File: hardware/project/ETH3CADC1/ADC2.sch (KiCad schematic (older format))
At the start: 45 parts, among them U401 DG211B, U402 OPA2192, U403 DG419xY, U404 LT5400-100k-100k, U405 LT5400-5k-1k, U406 OPA177, U407 OPA140, U408 OPA192, U409 LT5400-10k-10k, U410 LM311

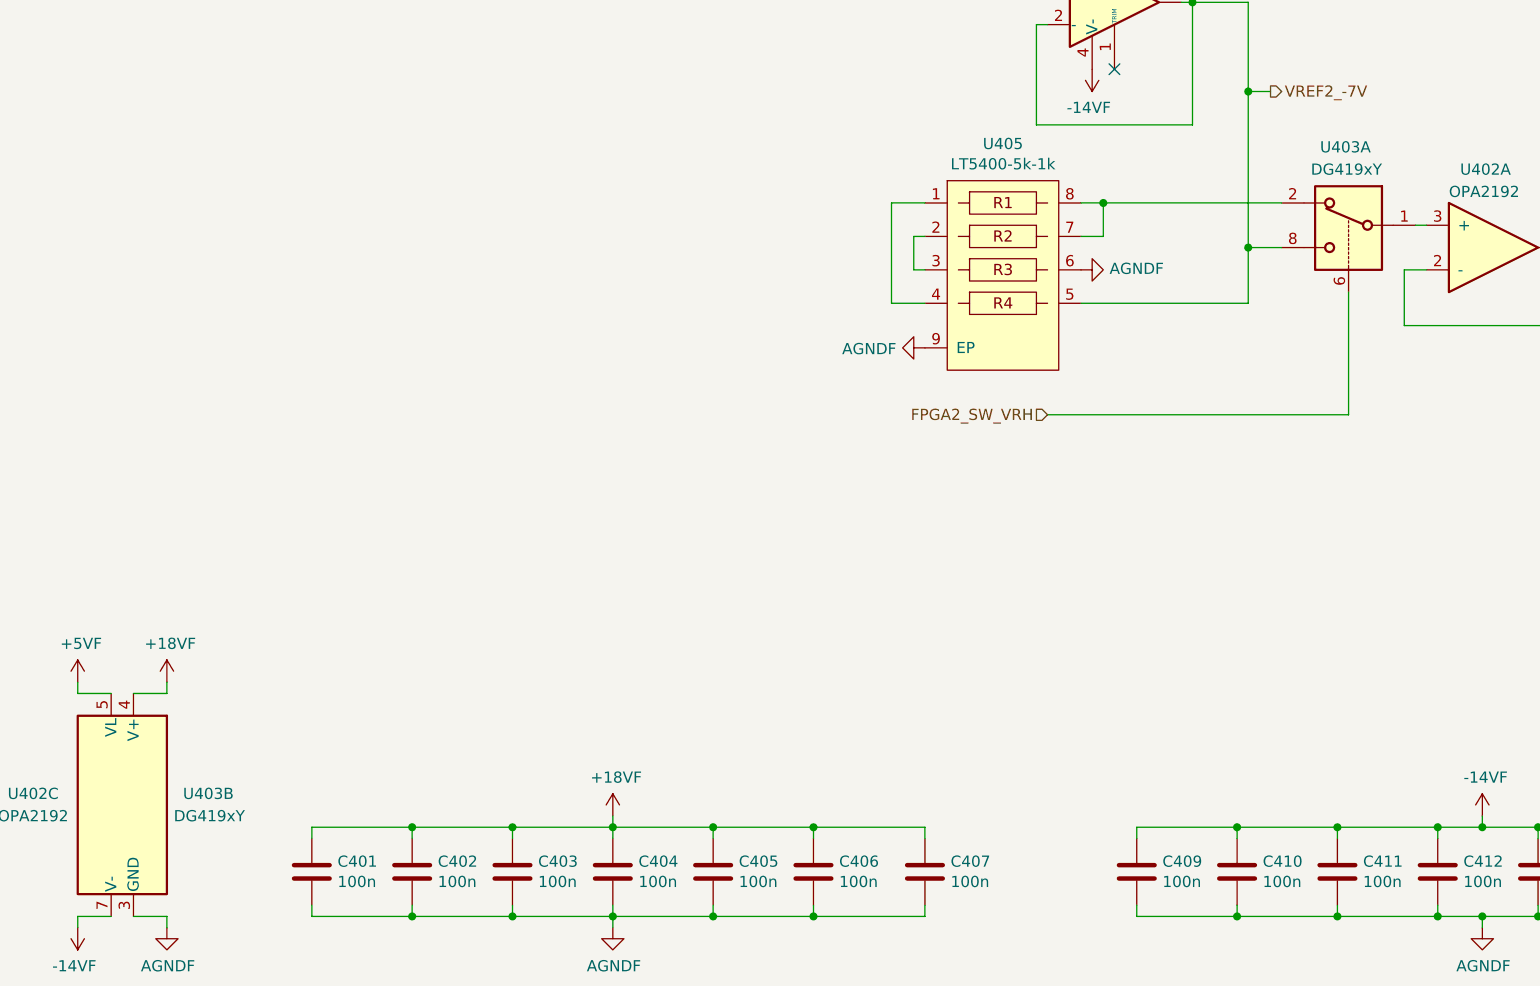
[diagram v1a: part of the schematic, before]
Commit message: Fixed mistake with DG419. Never use DG419Lxx variant.
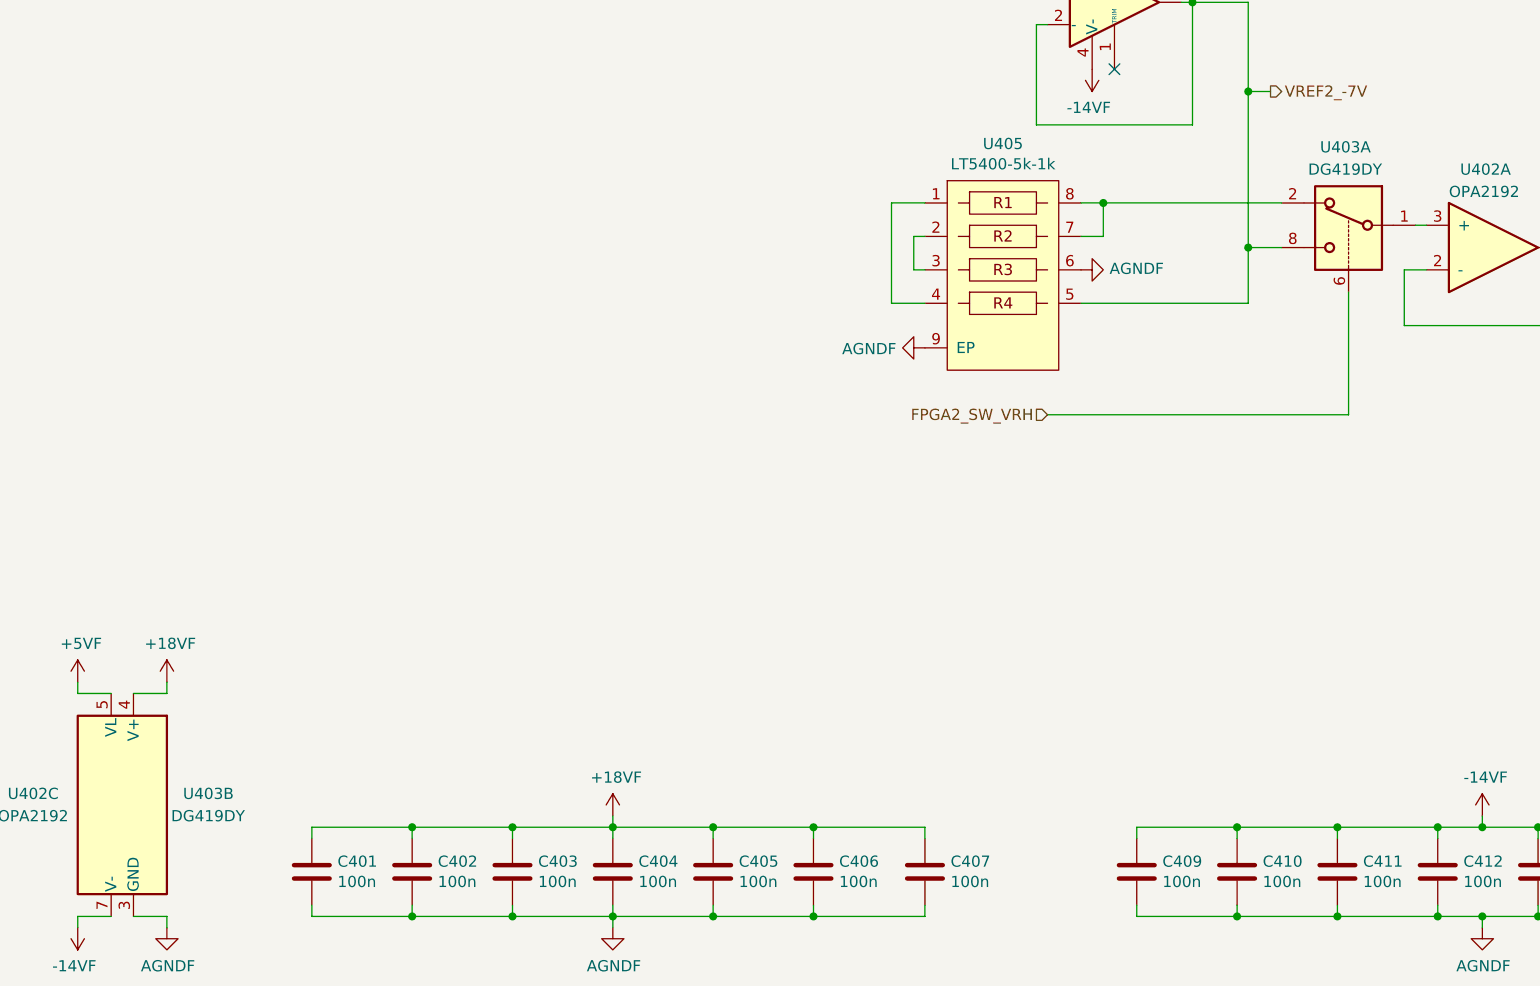
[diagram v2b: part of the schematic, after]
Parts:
- U403: value DG419xY -> DG419DY
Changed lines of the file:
@@
 AR Path="/605B15BF/6032E920" Ref="U?"  Part="1"
 F 0 "U403" H 8050 7650 50  0000 L CNN
-F 1 "DG419xY" H 8000 7550 50  0000 L CNN
+F 1 "DG419DY" H 8000 7550 50  0000 L CNN
 F 2 "Package_SO:SOIC-8_3.9x4.9mm_P1.27mm" H 8150 7100 50  0001 C CNN
 F 3 "https://datasheets.maximintegrated.com/en/ds/DG417-DG419.pdf" H 8150 7400 50  0001 C CNN
@@
 AR Path="/605B15BF/6032E9AE" Ref="U?"  Part="2"
 F 0 "U403" H 2250 10150 50  0000 L CNN
-F 1 "DG419xY" H 2200 10050 50  0000 L CNN
+F 1 "DG419DY" H 2200 10050 50  0000 L CNN
 F 2 "Package_SO:SOIC-8_3.9x4.9mm_P1.27mm" H 2700 9800 50  0001 C CNN
 F 3 "https://datasheets.maximintegrated.com/en/ds/DG417-DG419.pdf" H 2700 10100 50  0001 C CNN

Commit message: Development
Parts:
- removed C401, C402, C403, C404, C405, C406, C407, C409, C410, C411, C412, C414, C416, C417, C418, C419, C420, C421: 100n, Capacitor_SMD:C_0402_1005Metric_Pad0.74x0.62mm_HandSolder, symbol Device:C
- removed C408: 2n2/SMD, Capacitor_SMD:C_0603_1608Metric_Pad1.08x0.95mm_HandSolder, symbol Device:C
- removed C413: 33p, Capacitor_SMD:C_0402_1005Metric_Pad0.74x0.62mm_HandSolder, symbol Device:C
- removed C415: DNP, Capacitor_SMD:C_0402_1005Metric_Pad0.74x0.62mm_HandSolder, symbol Device:C
- removed D401, D402: BAV21W, Diode_SMD:D_SOD-123, symbol Device:D
- removed R401, R402, R404, R405, R409: 10, Resistor_SMD:R_0402_1005Metric_Pad0.72x0.64mm_HandSolder, symbol Device:R
- removed R403: 12k/.05%, Resistor_SMD:R_0603_1608Metric_Pad0.98x0.95mm_HandSolder, symbol Device:R
- removed R406: 62k, Resistor_SMD:R_0402_1005Metric_Pad0.72x0.64mm_HandSolder, symbol Device:R
- removed R407: 620/.05%, Resistor_SMD:R_0603_1608Metric_Pad0.98x0.95mm_HandSolder, symbol Device:R
- removed R408, R412: 3k9/.05%, Resistor_SMD:R_0603_1608Metric_Pad0.98x0.95mm_HandSolder, symbol Device:R
- removed R410: 62/.1%, Resistor_SMD:R_0603_1608Metric_Pad0.98x0.95mm_HandSolder, symbol Device:R
- removed R411: 39k/.05%, Resistor_SMD:R_0603_1608Metric_Pad0.98x0.95mm_HandSolder, symbol Device:R
- removed U401: DG211B, Package_SO:TSSOP-16_4.4x5mm_P0.65mm, symbol ETH3CDAQ1:DG211
- removed U402: OPA2192, Package_SO:SOIC-8_3.9x4.9mm_P1.27mm, symbol ETH3CDAQ1:OPA2192
- removed U403: DG419DY, Package_SO:SOIC-8_3.9x4.9mm_P1.27mm, symbol Analog_Switch:DG419xY
- removed U404: LT5400-100k-100k, Package_SO:MSOP-8-1EP_3x3mm_P0.65mm_EP1.73x1.85mm_ThermalVias, symbol ETH3CDAQ1:LT5400-100k-100k
- removed U405: LT5400-5k-1k, Package_SO:MSOP-8-1EP_3x3mm_P0.65mm_EP1.73x1.85mm_ThermalVias, symbol ETH3CDAQ1:LT5400-5k-1k
- removed U406: OPA177, Package_SO:SOIC-8_3.9x4.9mm_P1.27mm, symbol ETH3CDAQ1:OPA177
- removed U407: OPA140, Package_SO:SOIC-8_3.9x4.9mm_P1.27mm, symbol ETH3CDAQ1:OPA140
- removed U408: OPA192, Package_SO:SOIC-8_3.9x4.9mm_P1.27mm, symbol ETH3CDAQ1:OPA192
- removed U409: LT5400-10k-10k, Package_SO:MSOP-8-1EP_3x3mm_P0.65mm_EP1.73x1.85mm_ThermalVias, symbol ETH3CDAQ1:LT5400-10k-10k
- removed U410: LM311, Package_SO:SOIC-8_3.9x4.9mm_P1.27mm, symbol Comparator:LM311
- added C1401, C1402, C1403, C1404, C1405, C1406, C1407, C1408, C1409, C1411, C1412, C1413, C1414, C1415, C1417, C1418, C1419, C1420, C1421: 100n, Capacitor_SMD:C_0402_1005Metric_Pad0.74x0.62mm_HandSolder, symbol Device:C
- added C1410: 2n2/SMD, Capacitor_SMD:C_0603_1608Metric_Pad1.08x0.95mm_HandSolder, symbol Device:C
- added C1416: 33p, Capacitor_SMD:C_0402_1005Metric_Pad0.74x0.62mm_HandSolder, symbol Device:C
- added D1401, D1402: BAV21W, Diode_SMD:D_SOD-123, symbol Device:D
- added R1401, R1402, R1403, R1404, R1407: 10k, Resistor_SMD:R_0402_1005Metric_Pad0.72x0.64mm_HandSolder, symbol Device:R
- added R1405: 10M, Resistor_SMD:R_0603_1608Metric_Pad0.98x0.95mm_HandSolder, symbol Device:R
- added R1406: 0, Resistor_SMD:R_0402_1005Metric_Pad0.72x0.64mm_HandSolder, symbol Device:R
- added R1408, R1418: 62/.1%, Resistor_SMD:R_0603_1608Metric_Pad0.98x0.95mm_HandSolder, symbol Device:R
- added R1409, R1410, R1412, R1413, R1417: 10, Resistor_SMD:R_0402_1005Metric_Pad0.72x0.64mm_HandSolder, symbol Device:R
- added R1411: 12k/.05%, Resistor_SMD:R_0603_1608Metric_Pad0.98x0.95mm_HandSolder, symbol Device:R
- added R1414: 62k, Resistor_SMD:R_0402_1005Metric_Pad0.72x0.64mm_HandSolder, symbol Device:R
- added R1415: 620/.05%, Resistor_SMD:R_0603_1608Metric_Pad0.98x0.95mm_HandSolder, symbol Device:R
- added R1416, R1420: 3k9/.05%, Resistor_SMD:R_0603_1608Metric_Pad0.98x0.95mm_HandSolder, symbol Device:R
- added R1419: 39k/.05%, Resistor_SMD:R_0603_1608Metric_Pad0.98x0.95mm_HandSolder, symbol Device:R
- added U1401: DG211, Package_SO:TSSOP-16_4.4x5mm_P0.65mm, symbol ETH3CDAQ1:DG211
- added U1402: DG211B, Package_SO:TSSOP-16_4.4x5mm_P0.65mm, symbol ETH3CDAQ1:DG211
- added U1403: OPA2192, Package_SO:SOIC-8_3.9x4.9mm_P1.27mm, symbol ETH3CDAQ1:OPA2192
- added U1404: DG419DY, Package_SO:SOIC-8_3.9x4.9mm_P1.27mm, symbol Analog_Switch:DG419xY
- added U1405, U1409: OPA140, Package_SO:SOIC-8_3.9x4.9mm_P1.27mm, symbol ETH3CDAQ1:OPA140
- added U1406: LT5400-100k-100k, Package_SO:MSOP-8-1EP_3x3mm_P0.65mm_EP1.73x1.85mm_ThermalVias, symbol ETH3CDAQ1:LT5400-100k-100k
- added U1407: LT5400-5k-1k, Package_SO:MSOP-8-1EP_3x3mm_P0.65mm_EP1.73x1.85mm_ThermalVias, symbol ETH3CDAQ1:LT5400-5k-1k
- added U1408: OPA177, Package_SO:SOIC-8_3.9x4.9mm_P1.27mm, symbol ETH3CDAQ1:OPA177
- added U1410: LT5400-10k-10k, Package_SO:MSOP-8-1EP_3x3mm_P0.65mm_EP1.73x1.85mm_ThermalVias, symbol ETH3CDAQ1:LT5400-10k-10k
- added U1411: OPA192, Package_SO:SOIC-8_3.9x4.9mm_P1.27mm, symbol ETH3CDAQ1:OPA192
- added U1412: LM311, Package_SO:SOIC-8_3.9x4.9mm_P1.27mm, symbol Comparator:LM311
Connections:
- net +18VF: now also C1401.1, C1402.1, C1403.1, C1405.1, C1406.1, C1407.1, C1408.1, R1409.1, R1412.1, U1401.13 (V+), U1402.13 (V+), U1403.4 (V-), U1404.4 (V+), U1405.7 (V+), U1408.7 (V+)
- net -14VF: now also C1409.1, C1411.1, C1412.1, C1413.1, C1414.1, C1415.1, C1417.1, C1418.1, R1410.2, R1413.2, R1417.2, U1401.4 (V-), U1402.4 (V-), U1403.8 (V+), U1404.7 (V-), U1405.4 (V-), U1408.4 (V-)
- net ADIN2: now also R1401.2
- net AD_COMP2: now also R1420.2, U1412.7
- net AGNDF: now also C1401.2, C1402.2, C1403.2, C1404.2, C1405.2, C1406.2, C1407.2, C1408.2, C1409.2, C1411.2, C1412.2, C1413.2, C1414.2, C1415.2, C1417.2, C1418.2, R1402.2, R1405.2, R1415.2, U1401.5 (GND), U1402.5 (GND), U1403.6 (-), U1404.3 (GND), U1406.9 (EP), U1407.6, U1407.9 (EP), U1409.3 (+), U1410.9 (EP), U1411.3 (+)
- net DGNDF: now also C1419.2, C1420.2, U1412.1 (GND)
- net FGPA2_AD_ID: now also U1402.16
- net FGPA2_AD_IIN: now also U1402.1
- net FGPA2_AD_IRN: now also U1402.8
- net FGPA2_AD_IRP: now also U1402.9
- net FPGA2_SW_VRH: now also U1404.6
- net VREF+: now also U1403.7, U1406.4, U1410.1, U1410.2
- net VREF-: now also U1403.1, U1403.2 (-), U1406.3, U1410.3, U1410.4
- net VREF_N7V_LPF: now also R1404.2, R1408.2
- new net: R1406.1, R1407.2, U1405.2 (-), U1405.6
- new net: R1405.1, R1406.2, U1401.10, U1401.15, U1401.3, U1401.6, U1405.3 (+)
- new net: U1402.6, U1406.5
- new net: C1410.2, U1402.10, U1402.14, U1402.3, U1402.7, U1409.2 (-)
- new net: U1402.11, U1406.6
- new net: U1403.5 (+), U1410.5, U1410.6, U1410.7, U1410.8
- new net: C1410.1, R1411.2, U1402.15, U1409.6
- new net: U1403.3 (+), U1404.1
- new net: U1407.1, U1407.4
- new net: U1407.2, U1407.3
- new net: U1404.8, U1407.5, U1408.2 (-), U1408.6
- new net: U1404.2, U1407.7, U1407.8
- new net: C1416.2, D1401.2 (A), D1402.1 (K), R1411.1, R1414.2, U1411.2 (-)
- new net: R1413.1, U1411.4 (V-)
- new net: C1416.1, D1401.1 (K), D1402.2 (A), R1414.1, R1416.2, U1411.6
- new net: R1412.2, U1411.7 (V+)
- new net: R1401.1, U1401.2
- new net: R1404.1, U1401.14
- new net: R1403.1, U1401.11
- new net: R1402.1, U1401.7
- new net: C1404.1, R1408.1, U1408.3 (+)
- new net: R1410.1, U1409.4 (V-)
- new net: R1409.2, U1409.7 (V+)
- new net: R1407.1, U1406.8
- new net: R1415.1, U1412.3 (-)
- new net: C1421.2, R1417.1, U1412.4 (V-)
- new net: R1418.2, R1419.1, R1420.1
- new net: R1419.2, U1412.5 (BAL)
- new net: U1406.1, U1406.2
- new net: U1402.2, U1406.7
- new net: R1416.1, U1412.2 (+)
- new net +10VRF: R1403.2
- new net +3.3VF: C1419.1, C1420.1, C1421.1, R1418.1, U1401.12 (VL), U1402.12 (VL), U1404.5 (VL), U1412.8 (V+)
- new net FPGA2_MUX_ADIN: U1401.1
- new net FPGA2_MUX_GND: U1401.8
- new net FPGA2_MUX_N7V: U1401.16
- new net FPGA2_MUX_P10V: U1401.9
- no-connect marks 3 -> 5
